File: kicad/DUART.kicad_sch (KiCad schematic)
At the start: 7 parts, among them J10 PORTB serial, J2 DUART I/O, J9 PORTA serial, U11 68681, Y1 Crystal

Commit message: added footprints
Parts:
- J6: renamed from J9; footprint (none) -> Connector_PinSocket_2.54mm:PinSocket_1x06_P2.54mm_Vertical
- J7: renamed from J10; footprint (none) -> Connector_PinSocket_2.54mm:PinSocket_1x06_P2.54mm_Vertical
- J8: renamed from J2; footprint (none) -> Connector_PinSocket_2.54mm:PinSocket_1x20_P2.54mm_Vertical
- renumbered C12 to C18, C13 to C19, U11 to U15
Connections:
- net GND: no longer J8.11 (Pin_11)
- net RXDB: now also J8.4 (Pin_4); no longer J8.12 (Pin_12)
- net TXDB: now also J8.5 (Pin_5); no longer J8.13 (Pin_13)
- net OP4: now reaches J8.10 (Pin_10)
- net OP4: now also U15.27 (OP4)
- net IP0: now reaches J8.14 (Pin_14)
- net IP0: now also U15.7 (IP0)
- net IP1: now reaches J8.15 (Pin_15)
- net IP1: now also U15.4 (IP1)
- net IP2: now reaches J8.16 (Pin_16)
- net IP2: now also U15.36 (IP2)
- net IP3: now reaches J8.17 (Pin_17)
- net IP3: now also U15.2 (IP3)
- net IP4: now reaches J8.18 (Pin_18)
- net IP4: now also U15.39 (IP4)
- net IP5: now reaches J8.19 (Pin_19)
- net IP5: now also U15.38 (IP5)
- net OP0: now reaches J8.6 (Pin_6)
- net OP0: now also U15.29 (OP0)
- net OP1: now reaches J8.7 (Pin_7)
- net OP1: now also U15.12 (OP1)
- net OP2: now reaches J8.8 (Pin_8)
- net OP2: now also U15.28 (OP2)
- net OP3: now reaches J8.9 (Pin_9)
- net OP3: now also U15.13 (OP3)
- net OP5: now reaches U15.14 (OP5)
- net OP5: now also J8.11 (Pin_11)
- net OP7: now reaches U15.15 (OP7)
- net OP7: now also J8.13 (Pin_13)
- net OP6: now reaches U15.26 (OP6)
- net OP6: now also J8.12 (Pin_12)
- no-connect marks 33 -> 6
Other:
- moved on the sheet: J8

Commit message: updated readme
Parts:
- added C7: 100nF, Capacitor_THT:CP_Radial_D5.0mm_P2.50mm, symbol Device:C
- C19: renamed from C18; value C -> 7pF
- C20: renamed from C19; value C -> 7pF
- renumbered Y1 to 3.6864MHz1
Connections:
- net GND: now also C7.2
- net IP0: now also J8.2 (Pin_2); no longer J8.14 (Pin_14)
- net IP1: now also J8.3 (Pin_3); no longer J8.15 (Pin_15)
- net IP2: now also J8.4 (Pin_4); no longer J8.16 (Pin_16)
- net IP3: now also J8.5 (Pin_5); no longer J8.17 (Pin_17)
- net IP4: now also J8.6 (Pin_6); no longer J8.18 (Pin_18)
- net IP5: now also J8.7 (Pin_7); no longer J8.19 (Pin_19)
- net OP0: now also J8.12 (Pin_12); no longer J8.6 (Pin_6)
- net OP1: now also J8.13 (Pin_13); no longer J8.7 (Pin_7)
- net OP2: now also J8.14 (Pin_14); no longer J8.8 (Pin_8)
- net OP3: now also J8.15 (Pin_15); no longer J8.9 (Pin_9)
- net OP4: now also J8.16 (Pin_16); no longer J8.10 (Pin_10)
- net OP5: now also J8.17 (Pin_17); no longer J8.11 (Pin_11)
- net OP6: now also J8.18 (Pin_18); no longer J8.12 (Pin_12)
- net OP7: now also J8.19 (Pin_19); no longer J8.13 (Pin_13)
- net RXDA: now also J8.10 (Pin_10); no longer J8.2 (Pin_2)
- net RXDB: now also J8.8 (Pin_8); no longer J8.4 (Pin_4)
- net TXDA: now also J8.11 (Pin_11); no longer J8.3 (Pin_3)
- net TXDB: now also J8.9 (Pin_9); no longer J8.5 (Pin_5)
- net VCC: now also C7.1

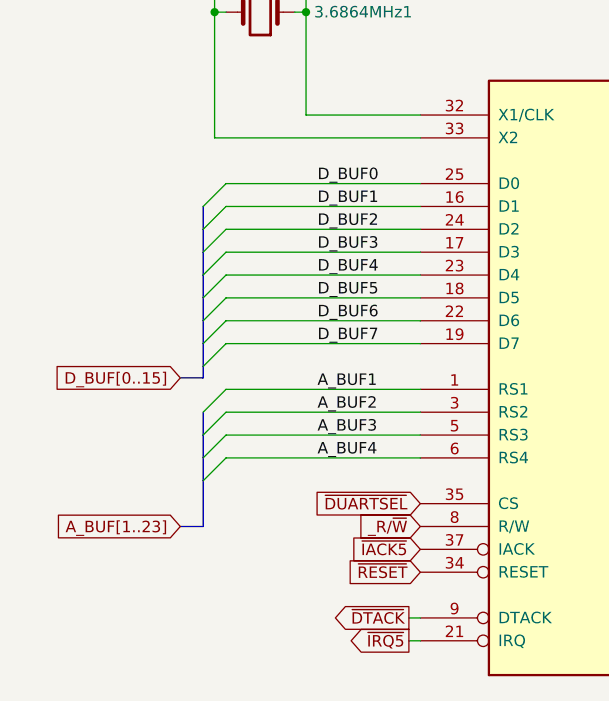
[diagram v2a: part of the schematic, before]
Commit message: PCB to ATX size
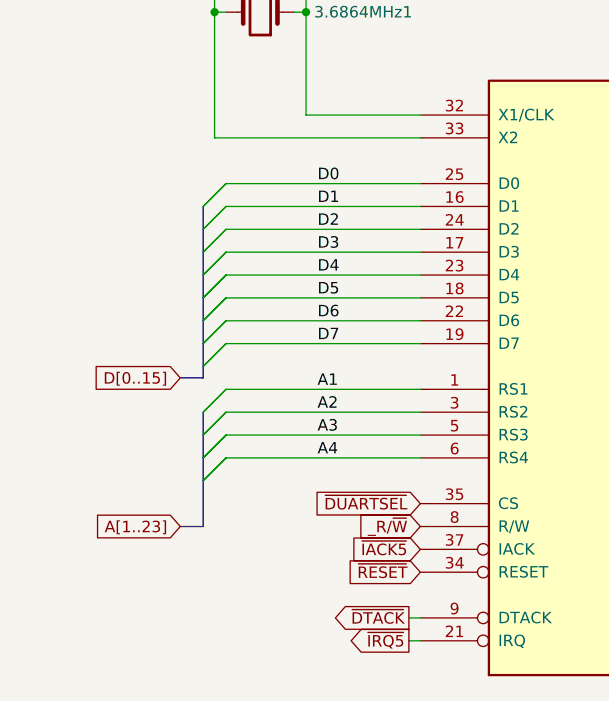
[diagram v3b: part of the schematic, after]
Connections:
- net A_BUF1 renamed A1
- net A_BUF2 renamed A2
- net A_BUF3 renamed A3
- net A_BUF4 renamed A4
- net D_BUF0 renamed D0
- net D_BUF1 renamed D1
- net D_BUF2 renamed D2
- net D_BUF3 renamed D3
- net D_BUF4 renamed D4
- net D_BUF5 renamed D5
- net D_BUF6 renamed D6
- net D_BUF7 renamed D7
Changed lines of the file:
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@@
+    (stroke (width 0) (type default))
+  )
+  (bus_entry (at 92.71 88.9) (size 2.54 -2.54)
     (stroke (width 0) (type default))
   )
@@
     (stroke (width 0) (type default))
   )
+  (bus_entry (at 92.71 83.82) (size 2.54 -2.54)
+    (stroke (width 0) (type default))
+  )
+  (bus_entry (at 92.71 73.66) (size 2.54 -2.54)
+    (stroke (width 0) (type default))
+  )
   (bus_entry (at 92.71 71.12) (size 2.54 -2.54)
     (stroke (width 0) (type default))
   )
+  (bus_entry (at 92.71 66.04) (size 2.54 -2.54)
+    (stroke (width 0) (type default))
+  )
+  (bus_entry (at 92.71 93.98) (size 2.54 -2.54)
+    (stroke (width 0) (type default))
+  )
+  (bus_entry (at 92.71 91.44) (size 2.54 -2.54)
+    (stroke (width 0) (type default))
+  )
   (bus_entry (at 92.71 96.52) (size 2.54 -2.54)
     (stroke (width 0) (type default))
   )
+  (bus_entry (at 92.71 81.28) (size 2.54 -2.54)
+    (stroke (width 0) (type default))
+  )
+  (bus_entry (at 92.71 76.2) (size 2.54 -2.54)
+    (stroke (width 0) (type default))
+  )
+  (bus_entry (at 92.71 96.52) (size 2.54 -2.54)
+    (stroke (width 0) (type default))
+  )
   (bus_entry (at 92.71 93.98) (size 2.54 -2.54)
     (stroke (width 0) (type default))
   )
+  (bus_entry (at 92.71 78.74) (size 2.54 -2.54)
+    (stroke (width 0) (type default))
+  )
   (bus_entry (at 92.71 91.44) (size 2.54 -2.54)
     (stroke (width 0) (type default))
@@
     (stroke (width 0) (type default))
   )
+  (bus_entry (at 92.71 68.58) (size 2.54 -2.54)
+    (stroke (width 0) (type default))
+  )
   (bus_entry (at 92.71 66.04) (size 2.54 -2.54)
     (stroke (width 0) (type default))
   )
+  (bus_entry (at 92.71 71.12) (size 2.54 -2.54)
+    (stroke (width 0) (type default))
+  )
   (bus_entry (at 92.71 88.9) (size 2.54 -2.54)
     (stroke (width 0) (type default))
@@
     (stroke (width 0) (type default))
   )
+  (wire (pts (xy 95.25 73.66) (xy 116.84 73.66))
+    (stroke (width 0) (type default))
+  )
   (wire (pts (xy 95.25 68.58) (xy 116.84 68.58))
     (stroke (width 0) (type default))
@@
     (stroke (width 0) (type default))
   )
+  (bus (pts (xy 92.71 78.74) (xy 92.71 81.28))
+    (stroke (width 0) (type default))
+  )
+  (bus (pts (xy 92.71 71.12) (xy 92.71 73.66))
+    (stroke (width 0) (type default))
+  )
+  (bus (pts (xy 92.71 68.58) (xy 92.71 71.12))
+    (stroke (width 0) (type default))
+  )
+  (wire (pts (xy 93.98 44.45) (xy 93.98 58.42))
+    (stroke (width 0) (type default))
+  )
+  (wire (pts (xy 95.25 78.74) (xy 116.84 78.74))
+    (stroke (width 0) (type default))
+  )
+  (wire (pts (xy 104.14 44.45) (xy 104.14 55.88))
+    (stroke (width 0) (type default))
+  )
+  (bus (pts (xy 92.71 93.98) (xy 92.71 96.52))
+    (stroke (width 0) (type default))
+  )
+  (wire (pts (xy 93.98 36.83) (xy 93.98 44.45))
+    (stroke (width 0) (type default))
+  )
+  (wire (pts (xy 95.25 88.9) (xy 116.84 88.9))
+    (stroke (width 0) (type default))
+  )
+  (bus (pts (xy 92.71 91.44) (xy 92.71 93.98))
+    (stroke (width 0) (type default))
+  )
+  (wire (pts (xy 95.25 93.98) (xy 116.84 93.98))
+    (stroke (width 0) (type default))
+  )
   (wire (pts (xy 95.25 71.12) (xy 116.84 71.12))
     (stroke (width 0) (type default))
   )
-  (wire (pts (xy 95.25 73.66) (xy 116.84 73.66))
-    (stroke (width 0) (type default))
-  )
-  (bus (pts (xy 92.71 78.74) (xy 92.71 81.28))
-    (stroke (width 0) (type default))
-  )
-  (bus (pts (xy 92.71 71.12) (xy 92.71 73.66))
-    (stroke (width 0) (type default))
-  )
-  (bus (pts (xy 92.71 68.58) (xy 92.71 71.12))
-    (stroke (width 0) (type default))
-  )
-  (wire (pts (xy 93.98 44.45) (xy 93.98 58.42))
-    (stroke (width 0) (type default))
-  )
-  (wire (pts (xy 95.25 78.74) (xy 116.84 78.74))
-    (stroke (width 0) (type default))
-  )
-  (wire (pts (xy 104.14 44.45) (xy 104.14 55.88))
-    (stroke (width 0) (type default))
-  )
-  (bus (pts (xy 92.71 93.98) (xy 92.71 96.52))
-    (stroke (width 0) (type default))
-  )
-  (wire (pts (xy 93.98 36.83) (xy 93.98 44.45))
-    (stroke (width 0) (type default))
-  )
-  (wire (pts (xy 95.25 88.9) (xy 116.84 88.9))
-    (stroke (width 0) (type default))
-  )
-  (bus (pts (xy 92.71 91.44) (xy 92.71 93.98))
-    (stroke (width 0) (type default))
-  )
-  (wire (pts (xy 95.25 93.98) (xy 116.84 93.98))
-    (stroke (width 0) (type default))
-  )
   (wire (pts (xy 95.25 91.44) (xy 116.84 91.44))
     (stroke (width 0) (type default))
@@
     (stroke (width 0) (type default))
   )
-  (label "A_BUF4" (at 105.41 93.98 0) (fields_autoplaced)
-    (effects (font (size 1.27 1.27)) (justify left bottom))
-  )
-  (label "D_BUF6" (at 105.41 78.74 0) (fields_autoplaced)
-    (effects (font (size 1.27 1.27)) (justify left bottom))
-  )
-  (label "A_BUF2" (at 105.41 88.9 0) (fields_autoplaced)
-    (effects (font (size 1.27 1.27)) (justify left bottom))
-  )
-  (label "D_BUF0" (at 105.41 63.5 0) (fields_autoplaced)
-    (effects (font (size 1.27 1.27)) (justify left bottom))
-  )
-  (label "D_BUF3" (at 105.41 71.12 0) (fields_autoplaced)
-    (effects (font (size 1.27 1.27)) (justify left bottom))
-  )
-  (label "A_BUF3" (at 105.41 91.44 0) (fields_autoplaced)
-    (effects (font (size 1.27 1.27)) (justify left bottom))
-  )
-  (label "D_BUF5" (at 105.41 76.2 0) (fields_autoplaced)
-    (effects (font (size 1.27 1.27)) (justify left bottom))
-  )
-  (label "D_BUF1" (at 105.41 66.04 0) (fields_autoplaced)
-    (effects (font (size 1.27 1.27)) (justify left bottom))
-  )
-  (label "A_BUF1" (at 105.41 86.36 0) (fields_autoplaced)
-    (effects (font (size 1.27 1.27)) (justify left bottom))
-  )
-  (label "D_BUF7" (at 105.41 81.28 0) (fields_autoplaced)
-    (effects (font (size 1.27 1.27)) (justify left bottom))
-  )
-  (label "D_BUF2" (at 105.41 68.58 0) (fields_autoplaced)
-    (effects (font (size 1.27 1.27)) (justify left bottom))
-  )
-  (label "D_BUF4" (at 105.41 73.66 0) (fields_autoplaced)
+  (label "D5" (at 105.41 76.2 0)
+    (effects (font (size 1.27 1.27)) (justify left bottom))
+  )
+  (label "D6" (at 105.41 78.74 0)
+    (effects (font (size 1.27 1.27)) (justify left bottom))
+  )
+  (label "A3" (at 105.41 91.44 0)
+    (effects (font (size 1.27 1.27)) (justify left bottom))
+  )
+  (label "A1" (at 105.41 86.36 0)
+    (effects (font (size 1.27 1.27)) (justify left bottom))
+  )
+  (label "D3" (at 105.41 71.12 0)
+    (effects (font (size 1.27 1.27)) (justify left bottom))
+  )
+  (label "D2" (at 105.41 68.58 0)
+    (effects (font (size 1.27 1.27)) (justify left bottom))
+  )
+  (label "A4" (at 105.41 93.98 0)
+    (effects (font (size 1.27 1.27)) (justify left bottom))
+  )
+  (label "A2" (at 105.41 88.9 0)
+    (effects (font (size 1.27 1.27)) (justify left bottom))
+  )
+  (label "D1" (at 105.41 66.04 0)
+    (effects (font (size 1.27 1.27)) (justify left bottom))
+  )
+  (label "D7" (at 105.41 81.28 0)
+    (effects (font (size 1.27 1.27)) (justify left bottom))
+  )
+  (label "D0" (at 105.41 63.5 0)
+    (effects (font (size 1.27 1.27)) (justify left bottom))
+  )
+  (label "D4" (at 105.41 73.66 0)
     (effects (font (size 1.27 1.27)) (justify left bottom))
   )
@@
     )
   )
-  (global_label "A_BUF[1..23]" (shape input) (at 90.17 101.6 180) (fields_autoplaced)
-    (effects (font (size 1.27 1.27)) (justify right))
-    (property "Intersheetrefs" "${INTERSHEET_REFS}" (at 74.9874 101.6 0)
+  (global_label "A[1..23]" (shape input) (at 90.17 101.6 180) (fields_autoplaced)
+    (effects (font (size 1.27 1.27)) (justify right))
+    (property "Intersheetrefs" "${INTERSHEET_REFS}" (at 79.6441 101.6 0)
       (effects (font (size 1.27 1.27)) (justify right) hide)
     )
@@
     )
   )
-  (global_label "D_BUF[0..15]" (shape input) (at 90.17 85.09 180) (fields_autoplaced)
-    (effects (font (size 1.27 1.27)) (justify right))
-    (property "Intersheetrefs" "${INTERSHEET_REFS}" (at 74.806 85.09 0)
-      (effects (font (size 1.27 1.27)) (justify right) hide)
-    )
+  (global_label "D[0..15]" (shape input) (at 90.17 85.09 180) (fields_autoplaced)
+    (effects (font (size 1.27 1.27)) (justify right))
+    (property "Intersheetrefs" "${INTERSHEET_REFS}" (at 79.4627 85.09 0)
+      (effects (font (size 1.27 1.27)) (justify right) hide)
+    )
